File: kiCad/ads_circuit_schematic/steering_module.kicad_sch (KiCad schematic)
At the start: 0 parts

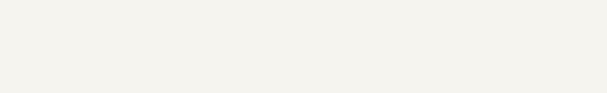
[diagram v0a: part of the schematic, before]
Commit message: Added new symbols for linear actuators, added fuses, added 5V step down
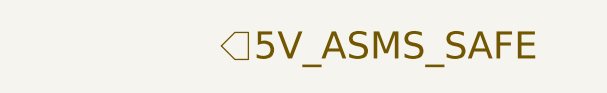
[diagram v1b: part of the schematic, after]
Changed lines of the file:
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@@
+		)
+	)
+	(hierarchical_label "5V_ASMS_SAFE"
+		(shape input)
+		(at 147.32 27.94 0)
+		(effects
+			(font
+				(size 3 3)
+				(color 255 0 0 1)
+			)
+			(justify left)
 		)
 	)

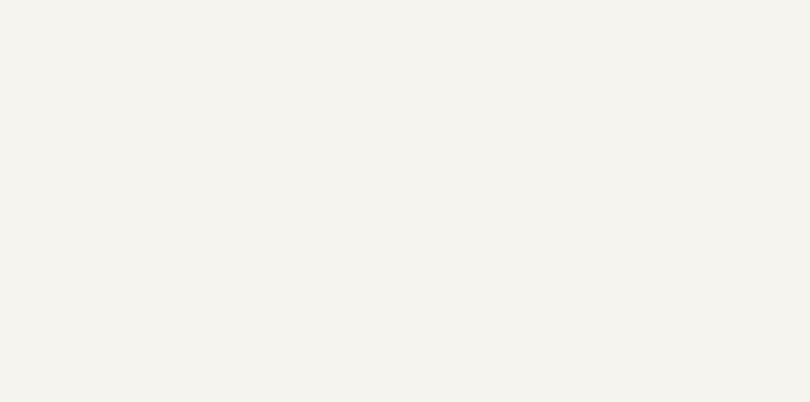
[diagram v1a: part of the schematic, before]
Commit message: made a new symbol for the steering motor in the steering module
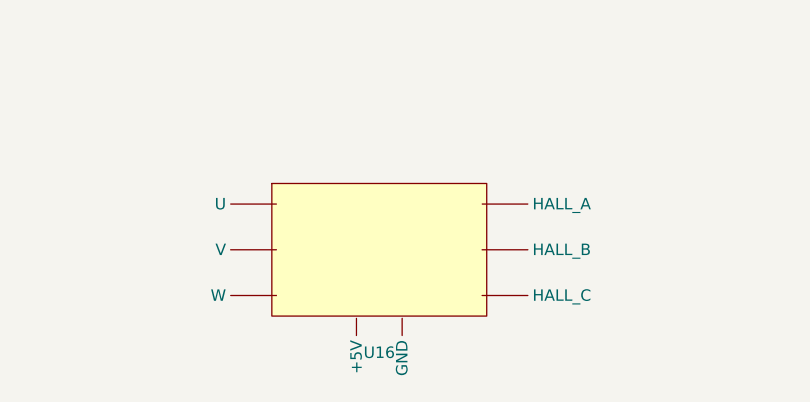
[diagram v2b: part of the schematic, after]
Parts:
- added U16: ~, symbol steering_motor:steering_motor
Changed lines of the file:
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@@
+		)
+	)
+	(symbol
+		(lib_id "steering_motor:steering_motor")
+		(at 137.16 80.01 0)
+		(unit 1)
+		(exclude_from_sim no)
+		(in_bom no)
+		(on_board yes)
+		(dnp no)
+		(fields_autoplaced yes)
+		(property "Reference" "U16"
+			(at 137.16 91.44 0)
+			(effects
+				(font
+					(size 1.27 1.27)
+				)
+			)
+		)
+		(property "Value" "~"
+			(at 137.16 93.98 0)
+			(effects
+				(font
+					(size 1.27 1.27)
+				)
+			)
+		)
+		(property "Footprint" ""
+			(at 137.16 80.01 0)
+			(effects
+				(font
+					(size 1.27 1.27)
+				)
+				(hide yes)
+			)
+		)
+		(property "Datasheet" ""
+			(at 137.16 80.01 0)
+			(effects
+				(font
+					(size 1.27 1.27)
+				)
+				(hide yes)
+			)
+		)
+		(property "Description" ""
+			(at 137.16 80.01 0)
+			(effects
+				(font
+					(size 1.27 1.27)
+				)
+				(hide yes)
+			)
+		)
+		(pin ""
+		)
+		(pin ""
+		)
+		(pin ""
+		)
+		(pin ""
+		)
+		(pin ""
+		)
+		(pin ""
+		)
+		(pin ""
+		)
+		(pin ""
+		)
+		(instances
+			(project ""
+				(path "/71fa6abf-14fe-4383-b55d-b9c0203d051b/cd0e913f-1e61-4dd3-b2d8-0b677d7a4880"
+					(reference "U16")
+					(unit 1)
+				)
+			)
 		)
 	)

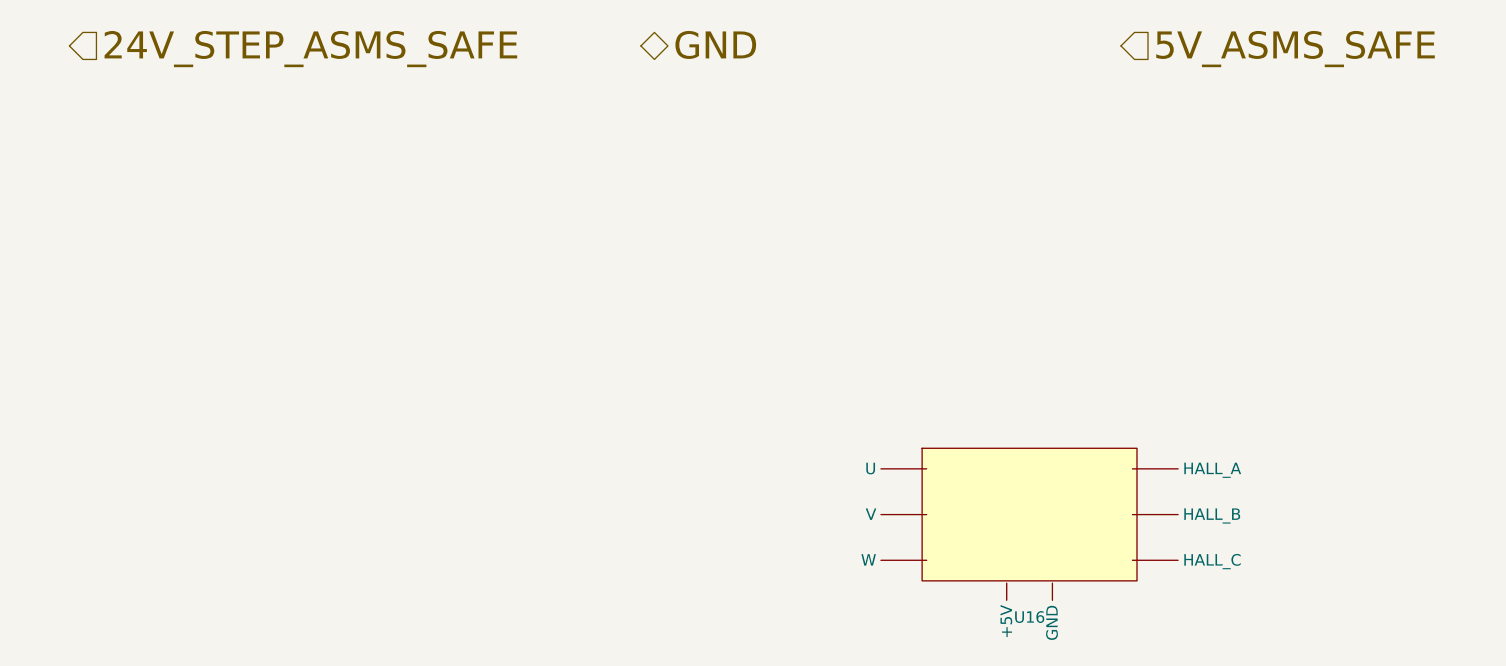
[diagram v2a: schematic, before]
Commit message: Added placeholder for steering motor driver
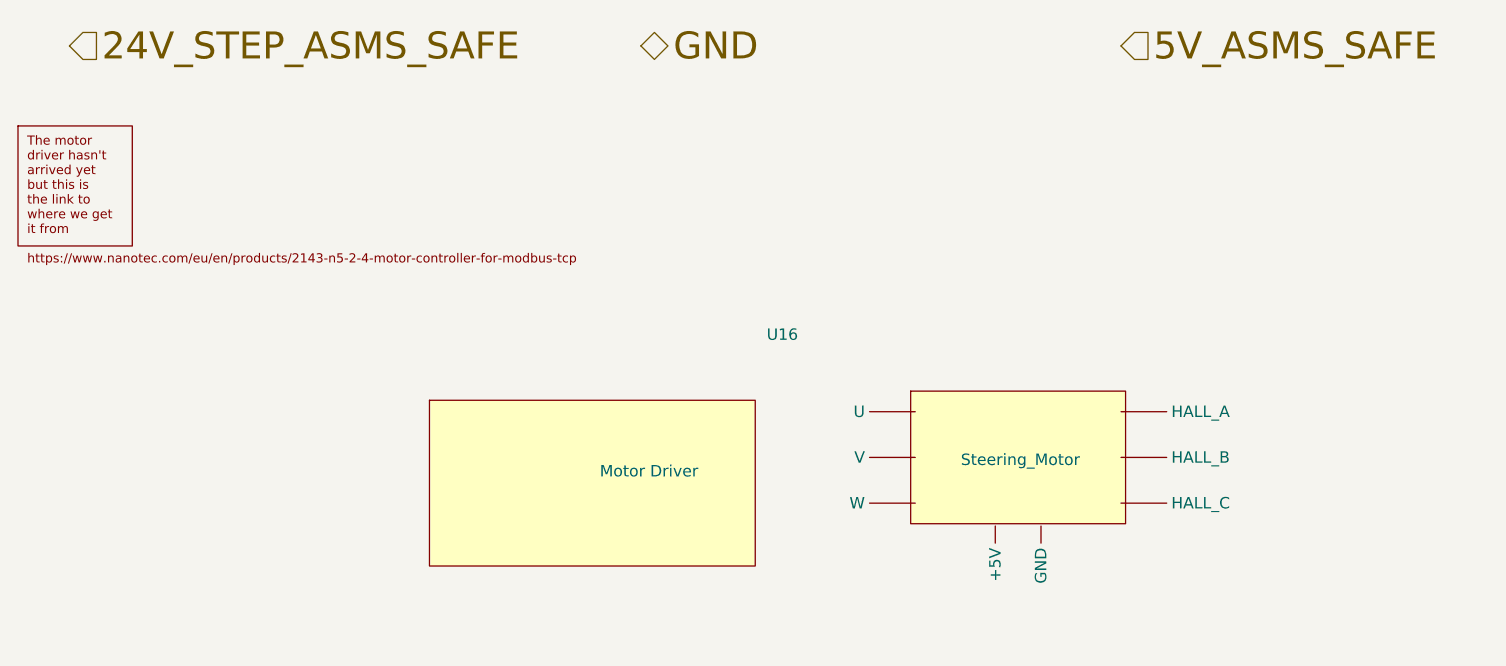
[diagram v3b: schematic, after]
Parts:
- added U16: Motor Driver, symbol steering_motor:motor_driver
- renumbered U16 to Steering_Motor
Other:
- moved on the sheet: Steering_Motor
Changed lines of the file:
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@@
 	(symbol
 		(lib_id "steering_motor:steering_motor")
-		(at 137.16 80.01 0)
+		(at 135.89 73.66 0)
 		(unit 1)
 		(exclude_from_sim no)
@@
 		(on_board yes)
 		(dnp no)
-		(fields_autoplaced yes)
-		(property "Reference" "U16"
-			(at 137.16 91.44 0)
+		(property "Reference" "Steering_Motor"
+			(at 136.144 73.914 0)
+			(effects
+				(font
+					(size 1.27 1.27)
+					(thickness 0.1588)
+				)
+			)
+		)
+		(property "Value" "~"
+			(at 135.89 87.63 0)
 			(effects
 				(font
 					(size 1.27 1.27)
 				)
-			)
-		)
-		(property "Value" "~"
-			(at 137.16 93.98 0)
-			(effects
-				(font
-					(size 1.27 1.27)
-				)
+				(hide yes)
 			)
 		)
 		(property "Footprint" ""
-			(at 137.16 80.01 0)
+			(at 135.89 73.66 0)
 			(effects
 				(font
@@
 		)
 		(property "Datasheet" ""
-			(at 137.16 80.01 0)
+			(at 135.89 73.66 0)
 			(effects
 				(font
@@
 		)
 		(property "Description" ""
-			(at 137.16 80.01 0)
+			(at 135.89 73.66 0)
 			(effects
 				(font
@@
 		)
 		(instances
+			(project ""
+				(path "/71fa6abf-14fe-4383-b55d-b9c0203d051b/cd0e913f-1e61-4dd3-b2d8-0b677d7a4880"
+					(reference "Steering_Motor")
+					(unit 1)
+				)
+			)
+		)
+	)
+	(symbol
+		(lib_id "steering_motor:motor_driver")
+		(at 88.9 78.74 0)
+		(unit 1)
+		(exclude_from_sim no)
+		(in_bom yes)
+		(on_board yes)
+		(dnp no)
+		(property "Reference" "U16"
+			(at 107.95 60.0074 0)
+			(effects
+				(font
+					(size 1.27 1.27)
+				)
+				(justify left)
+			)
+		)
+		(property "Value" "Motor Driver"
+			(at 89.408 75.184 0)
+			(effects
+				(font
+					(size 1.27 1.27)
+				)
+				(justify left)
+			)
+		)
+		(property "Footprint" ""
+			(at 88.9 78.74 0)
+			(effects
+				(font
+					(size 1.27 1.27)
+				)
+				(hide yes)
+			)
+		)
+		(property "Datasheet" ""
+			(at 88.9 78.74 0)
+			(effects
+				(font
+					(size 1.27 1.27)
+				)
+				(hide yes)
+			)
+		)
+		(property "Description" ""
+			(at 88.9 78.74 0)
+			(effects
+				(font
+					(size 1.27 1.27)
+				)
+				(hide yes)
+			)
+		)
+		(instances
